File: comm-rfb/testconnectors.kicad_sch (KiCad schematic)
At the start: 3 parts, among them J10 Conn_02x04_Counter_Clockwise, J11 Conn_02x06_Odd_Even, J12 Conn_02x05_Counter_Clockwise

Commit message: comm-rfb: reduce number of sheets in schematic
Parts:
- J10: footprint (none) -> Connector_PinSocket_2.54mm:PinSocket_2x04_P2.54mm_Vertical
- J11: footprint (none) -> Connector_PinSocket_2.54mm:PinSocket_2x06_P2.54mm_Horizontal
- J12: footprint (none) -> Connector_PinSocket_2.54mm:PinSocket_2x05_P2.54mm_Horizontal
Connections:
- net SWIM is gone; now on net GND: J12.3 (Pin_3)
- net 5V0: no longer names the net of J12.5 (Pin_5)
- net 5V0: no longer J12.6 (Pin_6)
- net RST renamed NRST
- no-connect marks 0 -> 2
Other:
- note added: "Programming Header"
- note added: "Radio Test Connector"
- note added: "System Test Connector"
- moved on the sheet: J10, J11

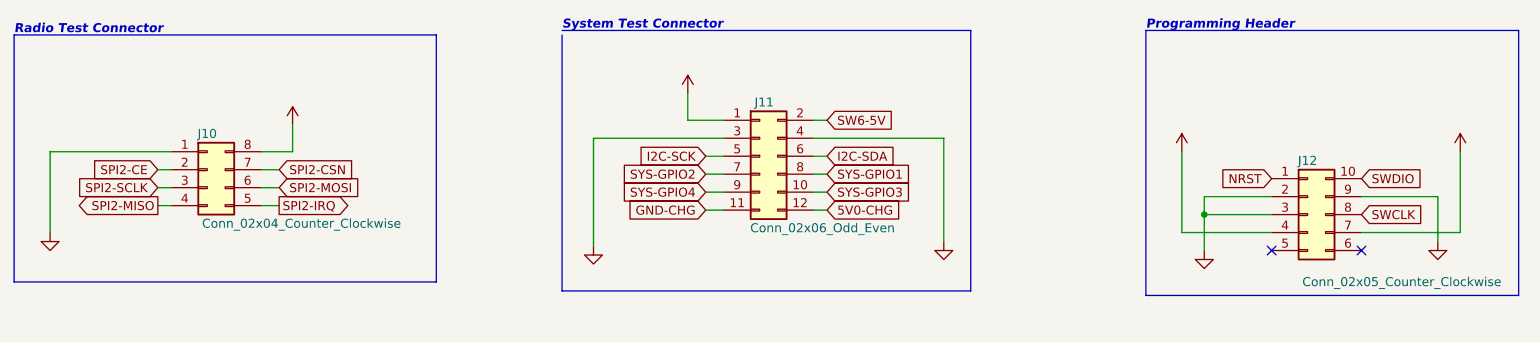
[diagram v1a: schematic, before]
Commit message: comm-rfb: reformat for rebase
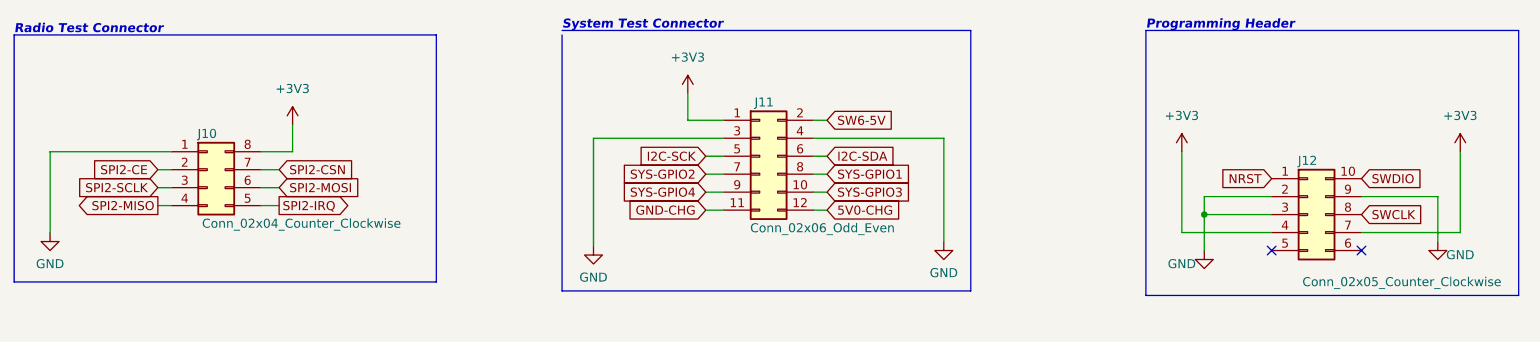
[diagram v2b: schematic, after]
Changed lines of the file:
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@@
       (effects (font (size 1.27 1.27)) hide)
     )
-    (property "Value" "" (id 1) (at 236.22 60.96 0))
+    (property "Value" "+3V3" (id 1) (at 236.22 60.96 0))
     (property "Footprint" "" (id 2) (at 236.22 66.04 0)
       (effects (font (size 1.27 1.27)) hide)
@@
       (effects (font (size 1.27 1.27)) hide)
     )
-    (property "Value" "" (id 1) (at 196.85 81.915 0))
+    (property "Value" "GND" (id 1) (at 196.85 81.915 0))
     (property "Footprint" "" (id 2) (at 200.025 80.01 0)
       (effects (font (size 1.27 1.27)) hide)
@@
       (effects (font (size 1.27 1.27)) hide)
     )
-    (property "Value" "" (id 1) (at 113.665 83.82 0))
+    (property "Value" "GND" (id 1) (at 113.665 83.82 0))
     (property "Footprint" "" (id 2) (at 113.665 79.375 0)
       (effects (font (size 1.27 1.27)) hide)
@@
       (effects (font (size 1.27 1.27)) hide)
     )
-    (property "Value" "" (id 1) (at 236.22 80.645 0))
+    (property "Value" "GND" (id 1) (at 236.22 80.645 0))
     (property "Footprint" "" (id 2) (at 233.045 78.74 0)
       (effects (font (size 1.27 1.27)) hide)
@@
       (effects (font (size 1.27 1.27)) hide)
     )
-    (property "Value" "" (id 1) (at 127 52.705 0))
+    (property "Value" "+3V3" (id 1) (at 127 52.705 0))
     (property "Footprint" "" (id 2) (at 127 57.785 0)
       (effects (font (size 1.27 1.27)) hide)
@@
       (effects (font (size 1.27 1.27)) hide)
     )
-    (property "Value" "" (id 1) (at 36.83 81.915 0))
+    (property "Value" "GND" (id 1) (at 36.83 81.915 0))
     (property "Footprint" "" (id 2) (at 36.83 77.47 0)
       (effects (font (size 1.27 1.27)) hide)
@@
       (effects (font (size 1.27 1.27)) hide)
     )
-    (property "Value" "" (id 1) (at 71.12 57.15 0))
+    (property "Value" "+3V3" (id 1) (at 71.12 57.15 0))
     (property "Footprint" "" (id 2) (at 71.12 62.23 0)
       (effects (font (size 1.27 1.27)) hide)
@@
       (effects (font (size 1.27 1.27)) hide)
     )
-    (property "Value" "" (id 1) (at 196.85 60.96 0))
+    (property "Value" "+3V3" (id 1) (at 196.85 60.96 0))
     (property "Footprint" "" (id 2) (at 196.85 66.04 0)
       (effects (font (size 1.27 1.27)) hide)
@@
       (effects (font (size 1.27 1.27)) hide)
     )
-    (property "Value" "" (id 1) (at 163.195 83.185 0))
+    (property "Value" "GND" (id 1) (at 163.195 83.185 0))
     (property "Footprint" "" (id 2) (at 163.195 78.74 0)
       (effects (font (size 1.27 1.27)) hide)

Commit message: comm-rfb: include correct spacing for cc1120-em connectors, remove traces
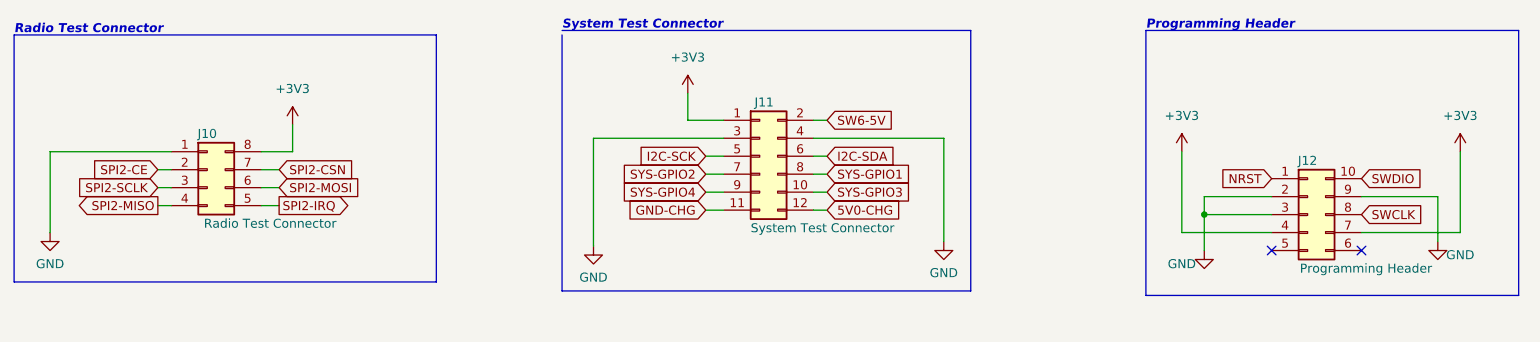
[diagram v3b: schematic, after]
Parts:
- J10: value Conn_02x04_Counter_Clockwise -> Radio Test Connector
- J11: value Conn_02x06_Odd_Even -> System Test Connector
- J12: value Conn_02x05_Counter_Clockwise -> Programming Header
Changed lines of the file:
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@@
     (in_bom yes) (on_board yes)
     (property "Reference" "J10" (id 0) (at 59.055 63.5 0))
-    (property "Value" "Conn_02x04_Counter_Clockwise" (id 1) (at 72.39 76.2 0))
+    (property "Value" "Radio Test Connector" (id 1) (at 67.945 76.2 0))
     (property "Footprint" "Connector_PinSocket_2.54mm:PinSocket_2x04_P2.54mm_Vertical" (id 2) (at 59.055 68.58 0)
       (effects (font (size 1.27 1.27)) hide)
@@
     (in_bom yes) (on_board yes)
     (property "Reference" "J11" (id 0) (at 137.795 59.055 0))
-    (property "Value" "Conn_02x06_Odd_Even" (id 1) (at 146.05 76.835 0))
+    (property "Value" "System Test Connector" (id 1) (at 146.05 76.835 0))
     (property "Footprint" "Connector_PinSocket_2.54mm:PinSocket_2x06_P2.54mm_Horizontal" (id 2) (at 137.16 66.675 0)
       (effects (font (size 1.27 1.27)) hide)
@@
     (in_bom yes) (on_board yes)
     (property "Reference" "J12" (id 0) (at 214.63 67.31 0))
-    (property "Value" "Conn_02x05_Counter_Clockwise" (id 1) (at 227.965 84.455 0))
+    (property "Value" "Programming Header" (id 1) (at 222.885 82.55 0))
     (property "Footprint" "Connector_PinSocket_2.54mm:PinSocket_2x05_P2.54mm_Horizontal" (id 2) (at 214.63 74.93 0)
       (effects (font (size 1.27 1.27)) hide)

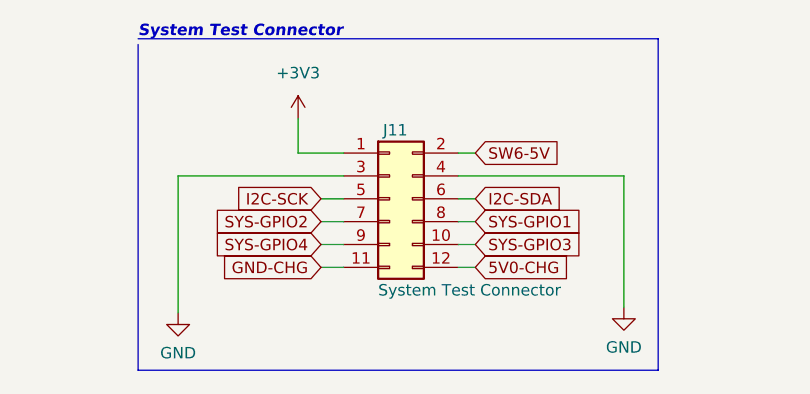
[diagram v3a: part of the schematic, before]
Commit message: comm-rfb: continue with new layout
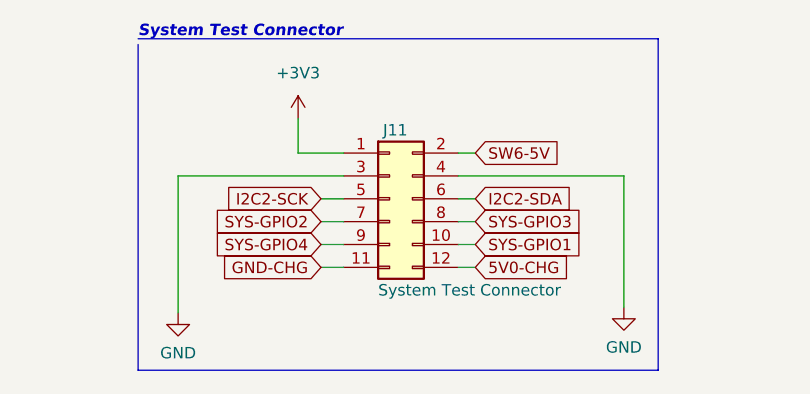
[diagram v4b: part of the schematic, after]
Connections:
- net SYS-GPIO1: now also J11.10 (Pin_10); no longer J11.8 (Pin_8)
- net SYS-GPIO3: now also J11.8 (Pin_8); no longer J11.10 (Pin_10)
- net I2C-SCK renamed I2C2-SCK
- net I2C-SDA renamed I2C2-SDA
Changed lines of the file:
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@@
     (effects (font (size 1.27 1.27) bold italic) (justify left bottom))
   )
-  (global_label "SYS-GPIO3" (shape input) (at 146.685 71.755 0) (fields_autoplaced)
+  (global_label "SYS-GPIO1" (shape input) (at 146.685 71.755 0) (fields_autoplaced)
     (effects (font (size 1.27 1.27)) (justify left))
     (property "Intersheet References" "${INTERSHEET_REFS}" (id 0) (at 159.8629 71.6756 0)
@@
     )
   )
-  (global_label "SYS-GPIO1" (shape input) (at 146.685 69.215 0) (fields_autoplaced)
+  (global_label "SYS-GPIO3" (shape input) (at 146.685 69.215 0) (fields_autoplaced)
     (effects (font (size 1.27 1.27)) (justify left))
     (property "Intersheet References" "${INTERSHEET_REFS}" (id 0) (at 159.8629 69.1356 0)
@@
     )
   )
-  (global_label "I2C-SDA" (shape input) (at 146.685 66.675 0) (fields_autoplaced)
+  (global_label "I2C2-SDA" (shape input) (at 146.685 66.675 0) (fields_autoplaced)
     (effects (font (size 1.27 1.27)) (justify left))
-    (property "Intersheet References" "${INTERSHEET_REFS}" (id 0) (at 157.3229 66.5956 0)
+    (property "Intersheet References" "${INTERSHEET_REFS}" (id 0) (at 158.5324 66.5956 0)
       (effects (font (size 1.27 1.27)) (justify left) hide)
     )
@@
     )
   )
-  (global_label "I2C-SCK" (shape input) (at 129.54 66.675 180) (fields_autoplaced)
+  (global_label "I2C2-SCK" (shape input) (at 129.54 66.675 180) (fields_autoplaced)
     (effects (font (size 1.27 1.27)) (justify right))
-    (property "Intersheet References" "${INTERSHEET_REFS}" (id 0) (at 118.7207 66.5956 0)
+    (property "Intersheet References" "${INTERSHEET_REFS}" (id 0) (at 117.5112 66.5956 0)
       (effects (font (size 1.27 1.27)) (justify right) hide)
     )

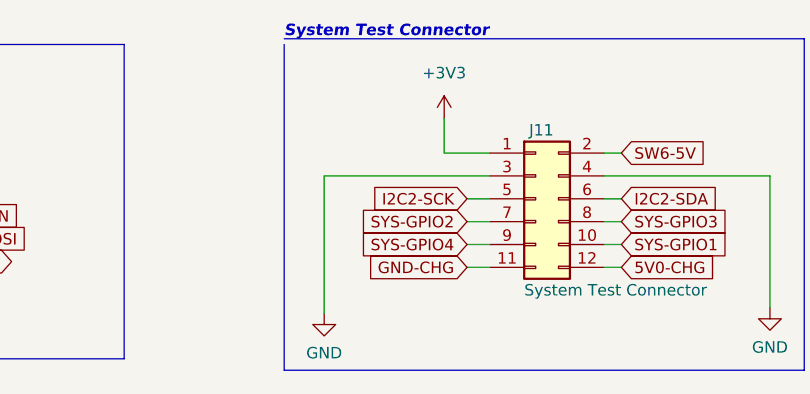
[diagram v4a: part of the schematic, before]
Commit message: comm-rfb: finish RF front end
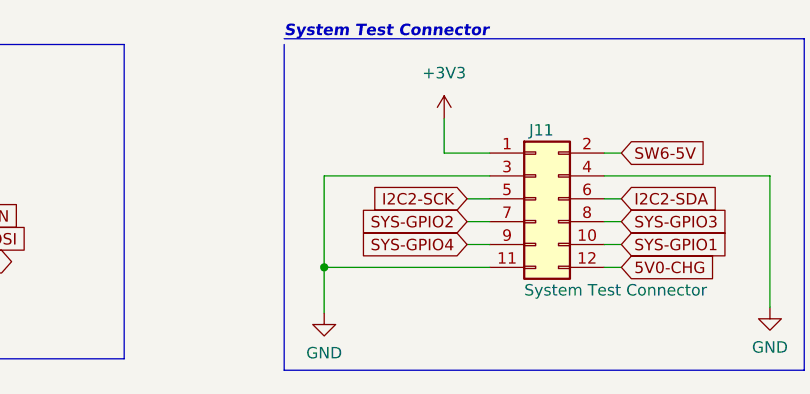
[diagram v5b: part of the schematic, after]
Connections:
- net GND-CHG is gone; now on net GND: J11.11 (Pin_11)
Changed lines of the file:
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@@
 (kicad_sch (version 20211123) (generator eeschema)
   (paper "A4")
+  (junction (at 113.665 74.295) (diameter 0) (color 0 0 0 0)
+  )
   (junction (at 200.025 74.93) (diameter 0) (color 0 0 0 0)
   )
@@
     (stroke (width 0) (type default) (color 0 0 0 0))
   )
-  (wire (pts (xy 129.54 74.295) (xy 132.08 74.295))
+  (wire (pts (xy 113.665 74.295) (xy 132.08 74.295))
     (stroke (width 0) (type default) (color 0 0 0 0))
   )
@@
     (stroke (width 0) (type default) (color 0 0 0 0))
   )
-  (wire (pts (xy 113.665 79.375) (xy 113.665 64.135))
+  (wire (pts (xy 113.665 79.375) (xy 113.665 74.295))
+    (stroke (width 0) (type default) (color 0 0 0 0))
+  )
+  (wire (pts (xy 113.665 74.295) (xy 113.665 64.135))
     (stroke (width 0) (type default) (color 0 0 0 0))
   )
@@
       (effects (font (size 1.27 1.27)) (justify right) hide)
     )
-  )
-  (global_label "GND-CHG" (shape input) (at 129.54 74.295 180) (fields_autoplaced)
-    (effects (font (size 1.27 1.27)) (justify right))
-    (property "Intersheet References" "${INTERSHEET_REFS}" (id 0) (at 117.8136 74.2156 0)
-      (effects (font (size 1.27 1.27)) (justify right) hide)
-    )
